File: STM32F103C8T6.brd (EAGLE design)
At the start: 20.3 x 50.8 mm, 38 parts, among them IC1 MCP170333MB, J1 455-1750-1-ND, J2 455-1750-1-ND, J4 CORTEX_DEBUG_MINIMUM_PTH, U1 STM32F103C8T6

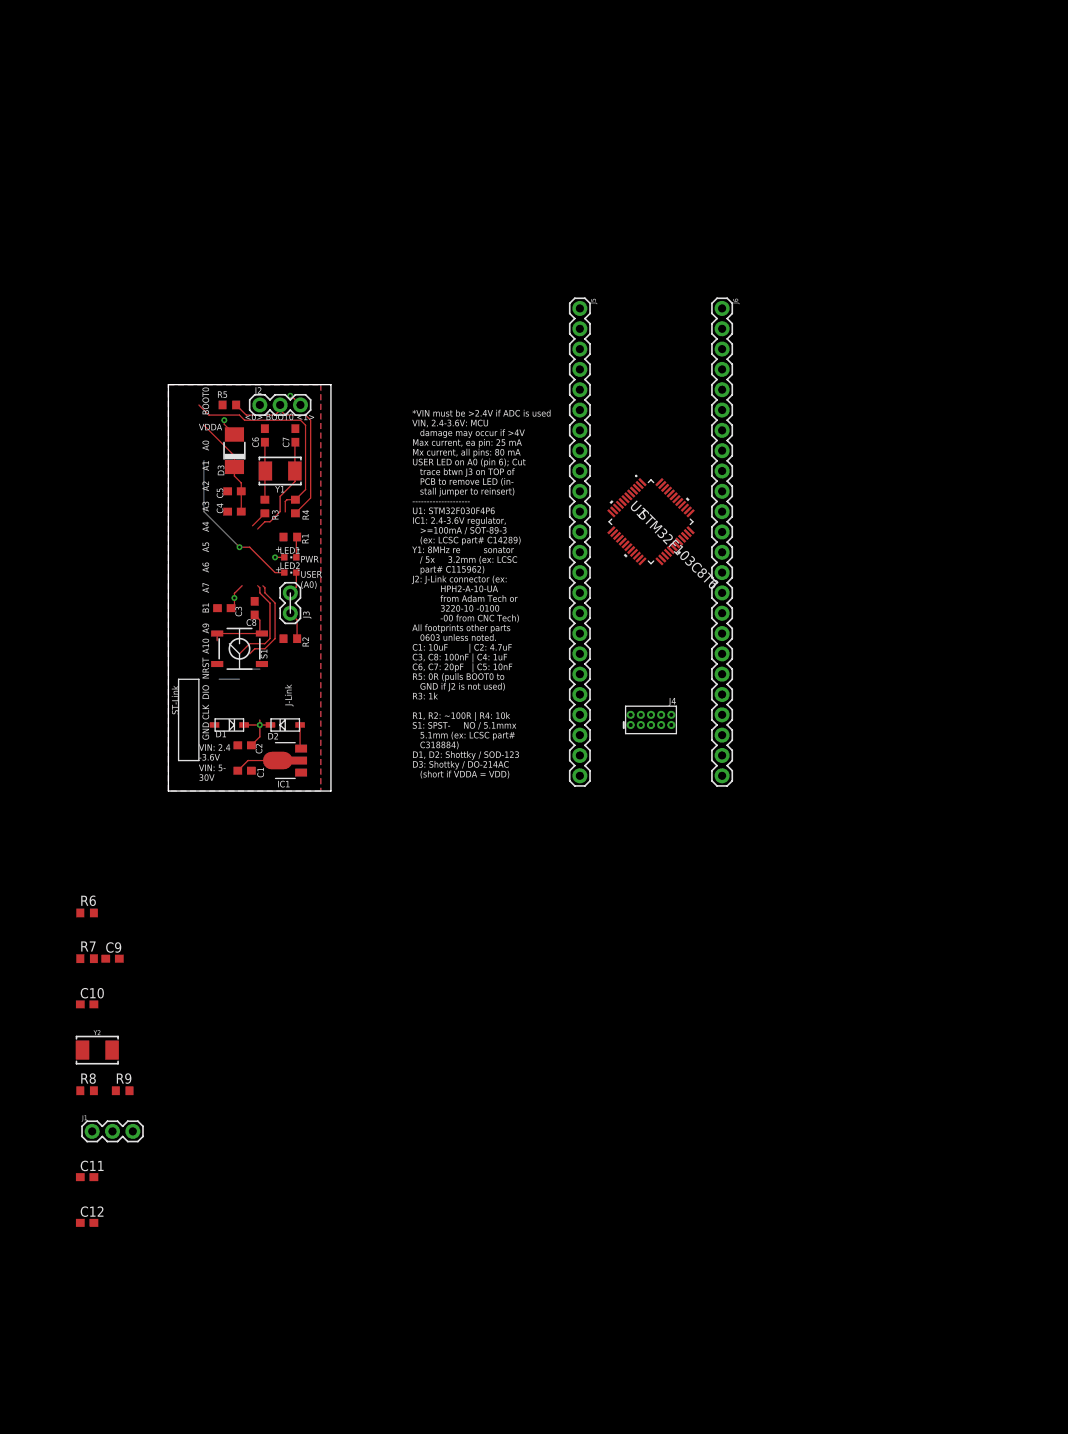
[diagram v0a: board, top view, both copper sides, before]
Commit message: Added power capacitors. Added new LSE oscillator.
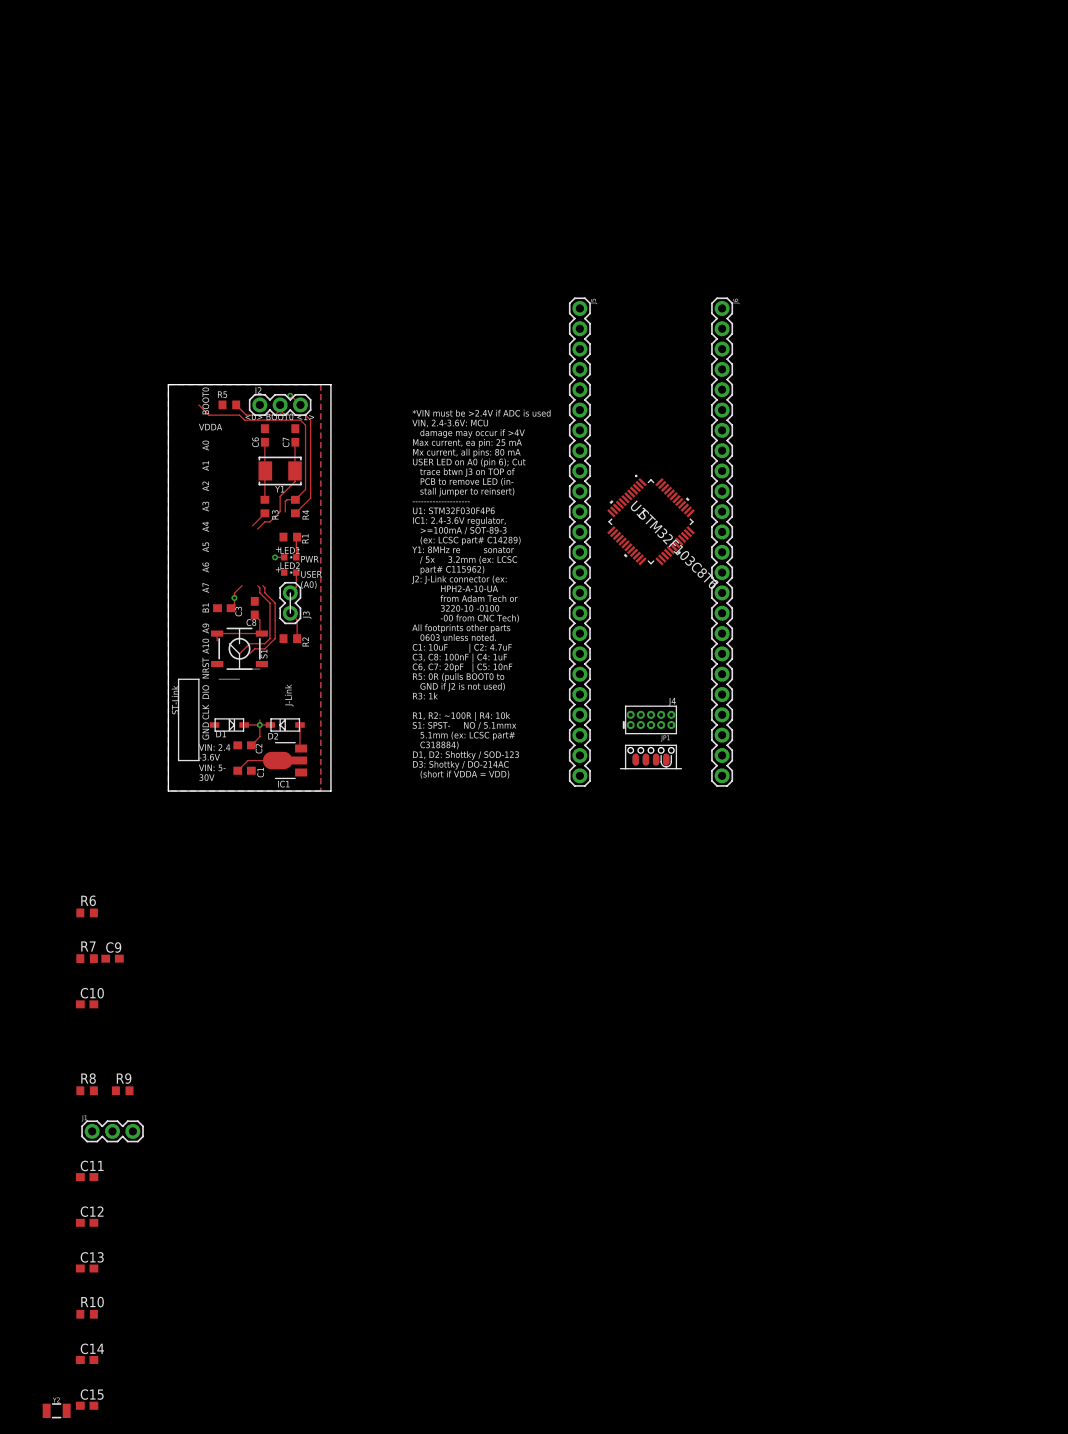
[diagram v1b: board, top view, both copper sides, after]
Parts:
- removed C4: 1uF, adafruit:C0603
- removed C5: 10nF, adafruit:C0603
- removed D3: (no value), diode:DO-214AC
- added C13, C15: 100nF, adafruit:C0603
- added C14: 1uF, adafruit:C0603
- added JP1: SOICBITE, SOICbite_Eagle:SOICBITE
- added R10: 0R, adafruit:R0603
- C2: value 4.7uF -> 10uF
- Y2: value (none) -> 32.768kHz; device SparkFun-Clocks:CRYSTAL-SMD-5X3.2-2PAD -> SparkFun-Clocks:CRYSTAL-SMD-3.2X1.5MM
- moved Y2 45.4 mm to (-14.0, -77.5)
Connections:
- removed net A0: LED2.A
- removed net JTDO: U1.39
- removed net VBAT_1.8-3.6V: R6.2, U1.1
- new net SWO: J4.6, U1.39
- new net VBAT: R6.1, U1.1
- net GND: now also C13.2, C14.2, C15.2; no longer C4.2, C5.2
- net N$4: now also Y2.P$2; no longer Y2.P$1
- net OSC32_IN: now also Y2.P$1; no longer Y2.P$2
- net VDD: now also C13.1, R10.2, R6.2; no longer D3.A, R6.1
- net VDDA: now also C14.1, C15.1, R10.1; no longer C4.1, C5.1, D3.C
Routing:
- net A0: track 20.0 -> 0.00 mm, vias 1 -> 0
- net VDDA: track 12.9 -> 0.00 mm
- net VDD: track 15.5 -> 13.2 mm, vias 5 -> 4

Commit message: Nearly finalized circuit.
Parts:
- removed C1, C2: 10uF, adafruit:C0603
- removed C10, C6, C7, C9: 20pF, adafruit:C0603
- removed C11, C12, C13, C15, C3, C8: 100nF, adafruit:C0603
- removed C14: 1uF, adafruit:C0603
- removed D1, D2: (no value), adafruit:SOD-123
- removed IC1: MCP170333MB, linear:SOT89
- removed JP1: SOICBITE, SOICbite_Eagle:SOICBITE
- removed R1: 100R, adafruit:R0603
- removed R10, R5, R6, R9: 0R, adafruit:R0603
- removed R3: 1k, adafruit:R0603
- removed R4, R8: 10k, adafruit:R0603
- added C16, C17, C18, C19, C25, C26: 100nF, adafruit:C0402
- added C20, C21: 30pF, adafruit:C0402
- added C22, C23: 15pF, adafruit:C0402
- added C24: 1uF, adafruit:C0402
- added C4, C5: 10uF, adafruit:C0402
- added D3, D4: (no value), adafruit:SOD-123
- added J7: AVX_009159010061916AVX_009159010061916_0_0, AVX - 009159010061916:AVX_009159010061916_0
- added R12: 100R, adafruit:R0402
- added R13, R15: 10k, adafruit:R0402
- added R14, R16, R18: 0R, adafruit:R0402
- added R17: 680R, adafruit:R0402
- added U2: CJT1117-3.3-SOT223, OPL_IC:SOT-223
- added USB1: 10118193-0001LF, OPL_Connector:MICRO-USB5+6P-SMD-0.65-B
- J4: value CORTEX_DEBUG_MINIMUM_PTH -> (none); device SparkFun-Connectors:2X5-PTH-1.27MM -> SparkFun-Connectors:1X02
- R7: value 1k -> 1k5; device adafruit:R0603 -> adafruit:R0402
- moved Y2 126.7 mm to (12.7, 46.4), turned to 180 degrees
- moved J1 83.6 mm to (31.1, 30.5)
- moved J5 50.5 mm to (1.27, 39.4)
- moved U1 48.0 mm to (12.7, 39.4)
- moved J6 45.4 mm to (24.1, 39.4)
- moved R7 41.3 mm to (20.3, 6.99), turned to 90 degrees
- moved J3 33.8 mm to (45.7, 36.8)
- moved LED1 33.8 mm to (45.7, 43.8)
- moved LED2 33.8 mm to (45.7, 41.9)
- moved R2 33.8 mm to (45.7, 33.7)
- moved S1 25.1 mm to (33.7, 21.6)
- moved J4 21.6 mm to (46.4, 25.4)
- moved J2 20.5 mm to (31.1, 42.5)
- moved Y1 9.03 mm to (6.99, 45.7), turned to 225 degrees
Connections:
- removed net BOOT1: R8.2, U1.20
- removed net JTDI: U1.38
- removed net JTRST: U1.40
- removed net N$4: C10.1, R7.1, Y2.P$2
- removed net N$5: D2.A, IC1.3
- removed net SWCLK: J4.4, U1.37
- removed net SWDIO: J4.2, U1.34
- removed net SWO: J4.6, U1.39
- removed net USB_DM: U1.32
- removed net USB_DP: U1.33
- removed net VBAT: R6.1, U1.1
- removed net VDDA: C14.1, C15.1, R10.1, U1.9
- removed net VIN_2-3.6V: D1.A
- removed net VIN_5-30V: C1.1, IC1.2@1
- new net BOOT1*: R15.2, U1.20
- new net JTDI*: J7.8, U1.38
- new net JTRST*: J7.9, U1.40
- new net PA0: U1.10
- new net PA1: U1.11
- new net PA10*: U1.31
- new net PA2: U1.12
- new net PA3: U1.13
- new net PA4: U1.14
- new net PA5: U1.15
- new net PA6: U1.16
- new net PA7: U1.17
- new net PA8*: U1.29
- new net PA9*: U1.30
- new net PB0: U1.18
- new net PB1: U1.19
- new net PB10*: U1.21
- new net PB11*: U1.22
- new net PB12*: U1.25
- new net PB13*: U1.26
- new net PB14*: U1.27
- new net PB15*: U1.28
- new net PB5: U1.41
- new net PB6*: U1.42
- new net PB7*: U1.43
- new net PB8*: U1.45
- new net PB9*: U1.46
- new net PC13: U1.2
- new net SWCLK*: J7.4, U1.37
- new net SWDIO*: J7.2, U1.34
- new net SWO*: J7.6, U1.39
- new net USB_DM*: U1.32, USB1.2
- new net USB_DP*: R7.1, U1.33, USB1.3
- new net VBAT_1.8-3.6V: C26.1, R18.1, U1.1
- new net VIN: C4.1, D3.C, D4.C, U2.3
- new net VIN_4.8-15V: D4.A
- new net VTREF: J7.1
- new net VUSB: D3.A, USB1.1
- net BOOT0: now also R13.2; no longer R4.2
- net GND: now also C16.2, C17.2, C18.2, C19.2, C20.2, C21.2, C22.2, C23.2, C24.2, C25.2, C26.2, C4.2, C5.2, J7.3, J7.5, R12.1, R14.1, R16.1, U2.1, USB1.4, USB1.5, USB1.S1, USB1.S2, USB1.S3, USB1.S4, USB1.S5, USB1.S6; no longer C1.2, C10.2, C11.2, C12.2, C13.2, C14.2, C15.2, C2.2, C3.2, C6.2, C7.2, C8.2, C9.2, IC1.1, J4.3, J4.5, J4.9, R1.1, R5.1, R9.1
- net N$1: now also R13.1, R14.2; no longer R4.1, R5.2
- net N$3: now also C21.1, R17.1; no longer C6.1, R3.1
- net N$6: now also R15.1, R16.2; no longer R8.1, R9.2
- net N$7: now also R12.2; no longer R1.2
- net NRST: now also C19.1, J7.10; no longer C8.1, J4.10
- net OSC32_IN: now also C22.1; no longer C9.1
- net OSC32_OUT: now also C23.1, Y2.P$2; no longer R7.2
- net OSC_IN: now also C20.1; no longer C7.1
- net OSC_OUT: now also R17.2; no longer R3.2
- net VDD: now also C16.1, C17.1, C18.1, C24.1, C25.1, C5.1, J4.2, R18.2, R7.2, U1.9, U2.2, U2.TER; no longer C11.1, C12.1, C13.1, C2.1, C3.1, D1.C, D2.C, R10.2, R6.2
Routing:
- net BOOT0: track 26.9 -> 0.00 mm
- net N$1: track 23.7 -> 0.00 mm
- net SWCLK: track 13.7 -> 0.00 mm
- net VDD: track 13.2 -> 0.00 mm, vias 4 -> 0
- net OSC_IN: track 13.2 -> 0.00 mm
- net SWDIO: track 11.8 -> 0.00 mm
- net NRST: track 11.6 -> 0.00 mm
- net N$2: track 8.92 -> 0.00 mm
- net N$3: track 7.24 -> 0.00 mm
- net VIN_5-30V: track 5.52 -> 0.00 mm
- net N$5: track 3.00 -> 0.00 mm
- net N$7: track 2.58 -> 0.00 mm
- net OSC_OUT: track 2.19 -> 0.00 mm
- removed copper zone on layer 1, net GND
- removed copper zone on layer 16, net VDD
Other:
- board size 20.3 x 50.8 mm -> 25.4 x 67.3 mm

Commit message: Nearly finished layout.
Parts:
- removed C16, C17, C18, C19, C25, C26: 100nF, adafruit:C0402
- removed C20, C21: 30pF, adafruit:C0402
- removed C22, C23: 15pF, adafruit:C0402
- removed C24: 1uF, adafruit:C0402
- removed D3, D4: (no value), adafruit:SOD-123
- removed R12: 100R, adafruit:R0402
- removed R13, R15: 10k, adafruit:R0402
- removed R14, R16, R18: 0R, adafruit:R0402
- removed R17: 680R, adafruit:R0402
- removed Y1: (no value), SparkFun-Clocks:CRYSTAL-SMD-5X3.2-2PAD
- removed Y2: 32.768kHz, SparkFun-Clocks:CRYSTAL-SMD-3.2X1.5MM
- added C1, C2: 10uF, adafruit:C0402
- added C10: 0.1uF, adafruit:C0402
- added C12: 01.uF, adafruit:C0402
- added C3, C7, C8, C9: 100nF, adafruit:C0402
- added C6: 1uF, adafruit:C0402
- added D1, D2: (no value), adafruit:SOD-123
- added J8: (no value), SparkFun-Connectors:1X02
- added Q1, Q2: (no value), crystal-geyer_V1_0:3.2X2.5_KXO-84-TCXO
- added R1: 1k5, adafruit:R0402
- added R4, R6: 10k, adafruit:R0402
- added R5: 0R, adafruit:R0402
- added R8, R9: 100R, adafruit:R0402
- C4, C5: value 10uF -> 100nF
- J1, J2: value 455-1750-1-ND -> (none); device SparkFun-Connectors:1X03 -> SparkFun-Connectors:1X19_NO_SILK
- J3: value (none) -> AVX_009159010061916AVX_009159010061916_0_0; device SparkFun-Connectors:1X02 -> AVX - 009159010061916:AVX_009159010061916_0
- J4: value (none) -> CORTEX_DEBUG_PTH; device SparkFun-Connectors:1X02 -> SparkFun-Connectors:2X5-PTH-1.27MM
- J5: device SparkFun-Connectors:1X24 -> SparkFun-Connectors:1X02
- J6: value (none) -> 455-1750-1-ND; device SparkFun-Connectors:1X24 -> SparkFun-Connectors:1X03
- J7: value AVX_009159010061916AVX_009159010061916_0_0 -> 455-1750-1-ND; device AVX - 009159010061916:AVX_009159010061916_0 -> SparkFun-Connectors:1X03
- R2: value 100R -> 0R; device adafruit:R0603 -> adafruit:R0402
- R7: value 1k5 -> 0R
- moved J7 50.1 mm to (14.0, 48.9), turned to 0 degrees
- moved J3 46.0 mm to (19.1, -0.64), turned to 180 degrees
- moved C4 42.3 mm to (17.1, 27.3)
- moved R7 42.2 mm to (11.4, 48.3), turned to 270 degrees
- moved LED1 41.5 mm to (5.08, 52.1), turned to 0 degrees
- moved LED2 38.8 mm to (8.26, 52.1), turned to 0 degrees
- moved J1 36.6 mm to (2.54, 53.3), turned to 270 degrees
- moved C5 36.1 mm to (19.7, 33.7)
- moved J4 35.8 mm to (14.6, 8.89)
- moved R2 26.7 mm to (19.1, 34.9), turned to 0 degrees
- moved J5 20.4 mm to (13.3, 22.9), turned to 180 degrees
- moved J6 15.8 mm to (14.0, 51.4), turned to 0 degrees
- moved S1 15.5 mm to (18.4, 19.1), turned to 90 degrees
- moved USB1 14.0 mm to (6.35, 4.45)
- moved J2 13.6 mm to (22.9, 53.3), turned to 270 degrees
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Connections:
- removed net N$2: J3.1, J3.2, LED2.C, R2.1
- removed net N$3: C21.1, R17.1, Y1.P$1
- removed net VTREF: J7.1
- new net N$4: LED2.A, R9.2
- new net VREG: J5.2, U2.2, U2.TER
- net BOOT0: now also R4.2; no longer R13.2
- net BOOT1*: now also R6.2; no longer R15.2
- net GND: now also C1.2, C10.2, C12.2, C2.2, C3.2, C6.2, C7.2, C8.2, C9.2, J2.17, J3.8, J3.9, J4.3, J4.5, J6.1, J7.1, LED1.C, LED2.C, Q1.2, Q2.2, R5.1, R7.1; no longer C16.2, C17.2, C18.2, C19.2, C20.2, C21.2, C22.2, C23.2, C24.2, C25.2, C26.2, J1.1, J2.1, J7.3, J7.5, R12.1, R14.1, R16.1, R2.2
- net JTDI*: now also J2.13, J3.2, J4.8; no longer J7.8
- net JTRST*: now also J2.12, J3.6, J4.9; no longer J7.9
- net N$1: now also J6.2, R4.1, R5.2; no longer J2.2, R13.1, R14.2
- net N$6: now also J7.2, R6.1, R7.2; no longer J1.2, R15.1, R16.2
- net N$7: now also LED1.A, R8.1; no longer LED1.C, R12.2
- net NRST: now also C9.1, J2.14, J3.1, J4.10; no longer C19.1, J7.10
- net OSC32_IN: now also Q2.3; no longer C22.1, Y2.P$1
- net OSC32_OUT: no longer C23.1, Y2.P$2
- net OSC_IN: now also Q1.3; no longer C20.1, Y1.P$2
- net OSC_OUT: no longer R17.2
- net PA0: now also J2.4
- net PA1: now also J2.3
- net PA10*: now also J1.16
- net PA2: now also J2.2
- net PA3: now also J2.1, J8.1, J8.2, R9.1
- net PA4: now also J1.1
- net PA5: now also J1.2
- net PA6: now also J1.3
- net PA7: now also J1.4
- net PA8*: now also J1.13
- net PA9*: now also J1.14
- net PB0: now also J1.5
- net PB1: now also J1.6
- net PB10*: now also J1.7
- net PB11*: now also J1.8
- net PB12*: now also J1.9
- net PB13*: now also J1.10
- net PB14*: now also J1.11
- net PB15*: now also J1.12
- net PB5: now also J2.11
- net PB6*: now also J2.10
- net PB7*: now also J2.9
- net PB8*: now also J2.8
- net PB9*: now also J2.7
- net PC13: now also J2.5
- net SWCLK*: now also J2.18, J3.4, J4.4; no longer J7.4
- net SWDIO*: now also J2.16, J3.5, J4.2; no longer J7.2
- net SWO*: now also J2.15, J3.3, J4.6; no longer J7.6
- net USB_DM*: now also J1.17
- net USB_DP*: now also J1.18, R1.1; no longer R7.1
- net VBAT_1.8-3.6V: now also C8.1, J2.6, R2.1; no longer C26.1, R18.1
- net VDD: now also C10.1, C12.1, C2.1, C3.1, C4.1, C6.1, C7.1, J2.19, J3.10, J5.1, J6.3, J7.3, Q1.4, Q2.4, R1.2, R2.2, R8.2; no longer C16.1, C17.1, C18.1, C24.1, C25.1, J1.3, J2.3, J4.2, LED1.A, R18.2, R7.2, U2.2, U2.TER
- net VIN: now also C1.1, D1.C, D2.C; no longer C4.1, D3.C, D4.C
- net VIN_4.8-15V: now also D2.A, J1.15; no longer D4.A
- net VUSB: now also D1.A, J1.19; no longer D3.A
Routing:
- net NRST: track 0.00 -> 44.1 mm, vias 0 -> 4
- net SWCLK*: track 0.00 -> 43.7 mm, vias 0 -> 1
- net SWDIO*: track 0.00 -> 42.5 mm, vias 0 -> 1
- net SWO*: track 0.00 -> 41.9 mm, vias 0 -> 2
- net JTRST*: track 0.00 -> 38.7 mm, vias 0 -> 1
- net JTDI*: track 0.00 -> 38.7 mm, vias 0 -> 3
- net PA3: track 0.00 -> 36.9 mm
- net VDD: track 0.00 -> 33.1 mm, vias 0 -> 9
- net USB_DP*: track 0.00 -> 31.6 mm, vias 0 -> 2
- net USB_DM*: track 0.00 -> 30.6 mm, vias 0 -> 1
- net PA2: track 0.00 -> 28.1 mm, vias 0 -> 1
- net GND: track 0.00 -> 23.9 mm, vias 0 -> 6
- net PA1: track 0.00 -> 23.2 mm, vias 0 -> 1
- net PA4: track 0.00 -> 23.0 mm
- net PA0: track 0.00 -> 21.2 mm, vias 0 -> 1
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- added copper zone on layer 1, net GND
- added copper zone on layer 16, net VDD
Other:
- board size 25.4 x 67.3 mm -> 24.1 x 55.2 mm
- board text added: "<0> BOOT1 <1>"
- board text added: "A11"
- board text added: "A12"
- board text added: "A3<->LED2"
- board text added: "A8"
- board text added: "B0"
- board text added: "B10"
- board text added: "B11"
- board text added: "B12"
- board text added: "B13"
- board text added: "B14"
- board text added: "B15"
- board text added: "B5"
- board text added: "B6"
- board text added: "B7"
- board text added: "B8"
- board text added: "B9"
- board text added: "BAT"
- board text added: "C13"
- board text added: "CUT LINE ABOVE TO DISCONNECT LED2 FROM PA3"
- board text added: "RESET"
- board text added: "SWO"
- board text added: "TDI"
- board text added: "TRST"
- board text added: "VDD"
- board text added: "VDD: 2-3.6V (>2.4V if ADC is used); MCU damage may occur if >4V VUSB: Output from USB1 (5V); diode-protected from VIN (both can be connected to power sources at the same time) VIN: 4.8-15V; diode-protected from VUSB (both can be connected to power sources at the same time) Place jumper on J5 to power MCU from VUSB or VIN; remove jumper to power from VDD. BAT: 1.8-3.6V; MCU battery backup. Short R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"
- board text added: "VIN"
- board text added: "VREG<->VDD"
- board text added: "VUSB"
- board text added: "|=5V tol."
- board text added: "~RST"
- board text removed: "(A0)"
- board text removed: "*VIN must be >2.4V if ADC is used VIN, 2.4-3.6V: MCU damage may occur if >4V Max current, ea pin: 25 mA Mx current, all pins: 80 mA USER LED on A0 (pin 6); Cut trace btwn J3 on TOP of PCB to remove LED (in- stall jumper to reinsert) -------------------- U1: STM32F030F4P6 IC1: 2.4-3.6V regulator, >=100mA / SOT-89-3 (ex: LCSC part# C14289) Y1: 8MHz re sonator / 5x 3.2mm (ex: LCSC part# C115962) J2: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"
- board text removed: "BOOT0"
- board text removed: "NRST"
- board text removed: "VDDA"
- board text removed: "VIN: 2.4 -3.6V"
- board text removed: "VIN: 5- 30V"

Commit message: Finished layout.
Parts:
- removed C12: 01.uF, adafruit:C0402
- removed R9: 100R, adafruit:R0402
- removed USB1: 10118193-0001LF, OPL_Connector:MICRO-USB5+6P-SMD-0.65-B
- added C11: 100nF, adafruit:C0402
- added R3: 10k, adafruit:R0402
- C10: value 0.1uF -> 100nF
- J3: value AVX_009159010061916AVX_009159010061916_0_0 -> AVX_6-PIN_009159006061916; device AVX - 009159010061916:AVX_009159010061916_0 -> Debug-Edge_AVX-connectors:AVX_6-PIN_009159006061916_0
- J5: value (none) -> 10118194-0001LF; device SparkFun-Connectors:1X02 -> USB-micro-B_Amphenol_10118194-0001LF:CONN_10118194-0001LF_AMP
- J6, J7: value 455-1750-1-ND -> (none); device SparkFun-Connectors:1X03 -> SparkFun-Connectors:1X03_NO_SILK
- J8: device SparkFun-Connectors:1X02 -> SparkFun-Connectors:1X02_NO_SILK
- R4, R6: value 10k -> 0R
- R5: value 0R -> 10k
- R7: value 0R -> 150R
- R8: value 100R -> 150R
- moved J5 22.5 mm to (6.35, 1.52), turned to 0 degrees
- moved R1 17.9 mm to (12.1, 24.8), turned to 0 degrees
- moved C2 13.4 mm to (14.6, 26.0), turned to 270 degrees
- moved R4 13.2 mm to (8.26, 52.1), turned to 90 degrees
- moved R6 7.96 mm to (8.26, 48.3), turned to 270 degrees
- moved R7 7.62 mm to (3.81, 48.3)
- moved R5 7.01 mm to (12.1, 45.1), turned to 0 degrees
- moved U2 4.49 mm to (7.62, 20.3)
- moved C1 4.07 mm to (10.2, 14.0)
- moved D1 4.02 mm to (6.35, 12.7), turned to 180 degrees
- moved J4 3.81 mm to (10.8, 8.89)
- moved C9 3.18 mm to (17.1, 13.3), turned to 90 degrees
- moved J2 3.18 mm to (19.7, 53.3)
- moved J6 3.18 mm to (10.8, 51.4)
- moved J7 3.18 mm to (10.8, 48.9)
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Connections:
- removed net VREG: J5.2, U2.2, U2.TER
- net BOOT0: now also R3.2; no longer R4.2
- net BOOT1*: now also R5.2; no longer R6.2
- net GND: now also C11.2, J3.6, J5.10, J5.11, J5.4, J5.5, J5.S_1, J5.S_1_H1, J5.S_1_H2, J5.S_2, J5.S_2_H1, J5.S_2_H2, J5.S_3, J5.S_3_H1, J5.S_3_H2, J5.S_4, J5.S_4_H1, J5.S_4_H2, R4.1, R6.1; no longer C12.2, J3.8, J3.9, R5.1, R7.1, USB1.4, USB1.5, USB1.S1, USB1.S2, USB1.S3, USB1.S4, USB1.S5, USB1.S6
- net JTDI*: no longer J3.2
- net JTRST*: no longer J3.6
- net N$1: now also R3.1, R4.2; no longer R4.1, R5.2
- net N$4: now also R8.2; no longer R9.2
- net N$6: now also R5.1, R6.2; no longer R6.1, R7.2
- net N$7: now also R7.1; no longer R8.1
- net NRST: now also J3.5; no longer J3.1
- net PA10*: now also J1.15; no longer J1.16
- net PA3: now also R8.1; no longer R9.1
- net SWCLK*: now also J3.2; no longer J3.4
- net SWDIO*: now also J3.1; no longer J3.5
- net USB_DM*: now also J5.2; no longer USB1.2
- net USB_DP*: now also J5.3; no longer USB1.3
- net VDD: now also C11.1, J3.4, R7.2, U2.2, U2.TER; no longer C12.1, J3.10, J5.1, R8.2
- net VIN_4.8-15V: now also J1.16; no longer J1.15
- net VUSB: now also J5.1; no longer USB1.1
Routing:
- net GND: track 23.9 -> 9.04 mm, vias 6 -> 2
- net VREG: track 11.8 -> 0.00 mm
- net JTDI*: track 38.7 -> 27.4 mm, vias 3 -> 2
- net JTRST*: track 38.7 -> 29.7 mm
- net PA2: track 28.1 -> 21.8 mm
- net VUSB: track 5.64 -> 11.4 mm
- net PA10*: track 18.5 -> 13.9 mm
- net PB9*: track 11.9 -> 7.29 mm, vias 0 -> 1
- net PB8*: track 9.23 -> 5.70 mm, vias 0 -> 1
- net PA1: track 23.2 -> 19.8 mm
- net PC13: track 15.5 -> 12.2 mm, vias 1 -> 2
- net PA0: track 21.2 -> 18.1 mm
- net VBAT_1.8-3.6V: track 11.9 -> 9.17 mm
- net SWDIO*: track 42.5 -> 40.2 mm
- net PB5: track 8.18 -> 5.91 mm
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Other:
- board size 24.1 x 55.2 mm -> 21.6 x 55.2 mm
- board text added: "-------POWER------- VDD: 2-3.6V. Must be 3.3V if C39097/ C387415 are used for Q1/Q2. VUSB: 5V from USB1 VIN: 4.8-15V BAT: 1.8-3.6V. Short R2 if unused. **WARNING**: Do NOT power MCU from VDD if EITHER VIN or USB1 are also being used. --------GPIO-------- Max current, ea pin: 25 mA Max current, total: 150 mA OUT (minus MCU power, ~7 -50 mA) and 150 mA IN (minus MCU power) Hor. bar = 5V tolerant pi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"
- board text added: "A3-LED2"
- board text added: "FMI: github.com/nathancharlesjones/STM32F103C8T6-breakout-board"
- board text added: "nRST"
- board text removed: "A3<->LED2"
- board text removed: "CUT LINE ABOVE TO DISCONNECT LED2 FROM PA3"
- board text removed: "FMI: github.com/nathancharlesjones/Embedded-for-Everyone/wiki"
- board text removed: "VDD: 2-3.6V (>2.4V if ADC is used); MCU damage may occur if >4V VUSB: Output from USB1 (5V); diode-protected from VIN (both can be connected to power sources at the same time) VIN: 4.8-15V; diode-protected from VUSB (both can be connected to power sources at the same time) Place jumper on J5 to power MCU from VUSB or VIN; remove jumper to power from VDD. BAT: 1.8-3.6V; MCU battery backup. Short R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"
- board text removed: "VREG<->VDD"
